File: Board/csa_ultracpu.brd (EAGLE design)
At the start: 160 x 100.1 mm, 131 parts, among them IC1 RAMSOCK32TO512KSOP, IC10 RAMSOCK32TO512KSOP, IC11 74HCT574D, IC12 74HCT574D, IC13 74HCT244DW, IC14 74HCT14D, IC15 74HCT157D, IC18 74LS06D, IC19 74HCT244DW, IC2 74LS245DW, IC3 74LS245DW, IC4 74LS245DW, IC5 74LS245DW, IC6 74ACT138D, IC7 74LS245DW, IC8 MAX3421E, IC9 74LS166D, P1 CSABUS, Q2 32kHz, Q3 12MHz, X2 D-SUB15-HDR15RA

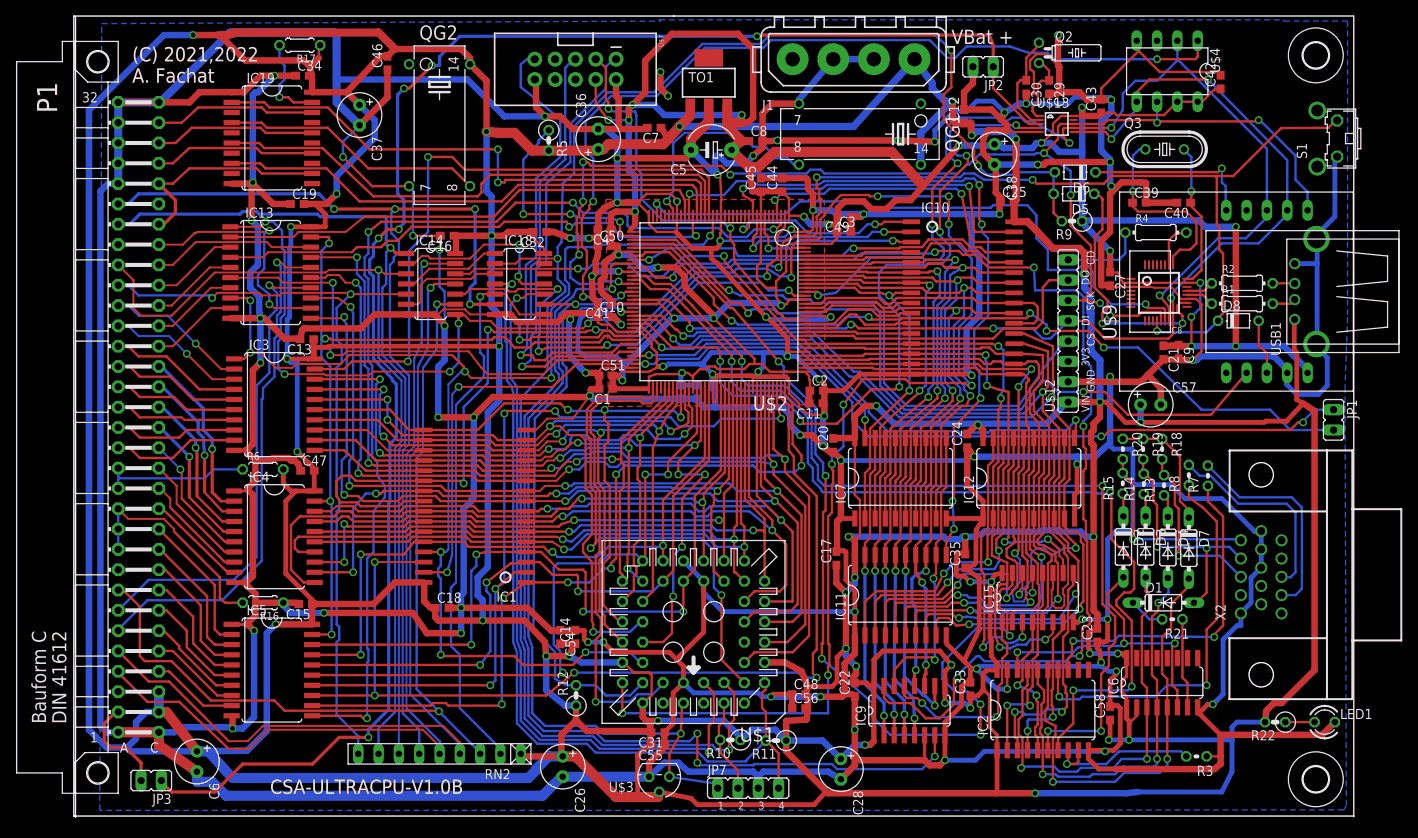
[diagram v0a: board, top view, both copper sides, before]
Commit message: update board to 1.3C
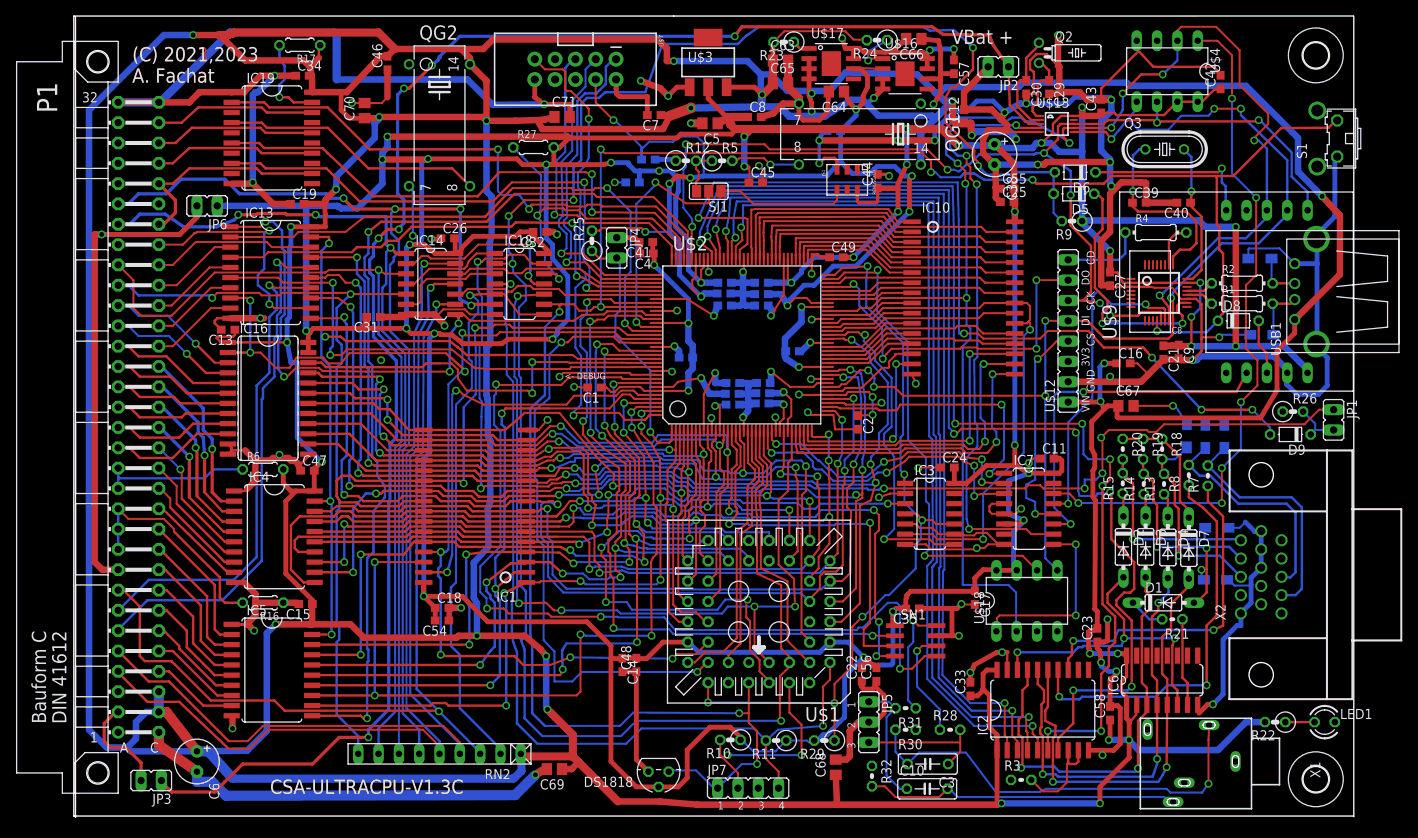
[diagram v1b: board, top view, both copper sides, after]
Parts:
- removed C20, C52: 0.1u, rcl:C0603
- removed C28, C36, C37: 22u, rcl:E2,5-6
- removed C50, C51, C53: 1u, rcl:C0603
- removed IC11, IC12: 74HCT574D, 74xx-eu:SO20W
- removed IC15: 74HCT157D, 74xx-eu:SO16
- removed IC9: 74LS166D, 74xx-eu:SO16
- removed J1: (no value), con-amp:350211
- removed TO1: LM2937SOT-3.3V, csa:SOT223
- added C100, C101, C102, C103, C104, C105, C106, C107, C108, C109, C110, C111, C112, C113: 0.1u, rcl:C0603
- added C120, C121, C123: 1u, rcl:C0603
- added C63, C64, C65, C66, C67, C68, C69, C70, C71: 22u, rcl:C0805
- added D9: 1N4148, diode:D-5
- added DS1818: DS1818, csa:TO92
- added IC16: 74LVC8T245SO24, csa:SO24L
- added JP4, JP6: (no value), jumper:JP1
- added JP5: (no value), jumper:JP2
- added JS1: RENOSCXLH, csa:RENJS6
- added R23, R24, R26: 10k, rcl:0207/2V
- added R25: 4k7, rcl:0207/2V
- added R27: 10k, rcl:0204/5
- added R28, R31: 100, rcl:0204V
- added R29: 330, rcl:0207/2V
- added R30, R32: 680, rcl:0204V
- added SJ1: (no value), jumper:SJ_2
- added SN1: MCP48X2, csa:SOIC8
- added U$10, U$11, U$14, U$15, U$5, U$6, U$8: PESD5V0L1BA, csa:SOD323
- added U$16: AP2132B-1.2, csa:PSOP-8-FIXED
- added U$17: AP2132B-2.5, csa:PSOP-8-FIXED
- added U$18: SPIFLASH, csa:DIL08
- added X1: SJ1-3513N, con-lumberg:1503_09
- C1, C14, C4: value 0.1u -> 1u
- C10: device rcl:C0603 -> rcl:C050-025X075
- C11: value 1u -> 0.1u
- C26: value 47u -> 0.1u; device rcl:E2,5-6 -> rcl:C0603
- C3: value 0.1u -> 1u; device rcl:C0603 -> rcl:C050-025X075
- C5: value 47u -> 22u; device rcl:E5-6 -> rcl:C0805
- C57: value 22u -> 1u; device rcl:E2,5-6 -> rcl:C0603
- IC14: value 74HCT14D -> 74LVC14
- IC18: value 74LS06D -> 74LVC06
- IC2, IC4, IC5: value 74LS245DW -> 74HCT245DW
- IC3: value 74LS245DW -> 74LS125D; device 74xx-eu:SO20W -> 74xx-eu:SO14
- IC6: value 74ACT138D -> 74HC138D
- IC7: value 74LS245DW -> 74S138D; device 74xx-eu:SO20W -> 74xx-eu:SO16
- R12: value 1k -> 1k5
- U$2: value XC95288XLTQ144 -> XC3S250E
- U$3: value DS1813 -> LDI1117; device csa:TO92 -> csa:SOT223
- moved U$3 88.2 mm to (78.7, 93.7), turned to 0 degrees
- moved C16 86.0 mm to (130.6, 56.1), turned to 0 degrees
- moved IC3 83.0 mm to (106.4, 37.3)
- moved C55 82.1 mm to (116.0, 77.9), turned to 0 degrees
- moved C10 71.4 mm to (106.0, 2.94)
- moved R12 68.2 mm to (75.9, 81.4), turned to 0 degrees
- moved C26 67.6 mm to (46.1, 71.8), turned to 0 degrees
- moved C3 67.3 mm to (106.1, 6.03), turned to 180 degrees
- moved C31 62.9 mm to (36.8, 61.9)
- moved C57 48.9 mm to (109.4, 93.2), turned to 270 degrees
- moved C11 29.7 mm to (121.0, 44.2), turned to 0 degrees
- moved R3 22.1 mm to (117.8, 4.05), turned to 0 degrees
- moved R5 21.8 mm to (80.4, 81.4), turned to 0 degrees
- moved C48 20.6 mm to (69.7, 18.4), turned to 90 degrees
- moved C17 18.0 mm to (112.0, 26.8), turned to 270 degrees
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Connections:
- removed net /CHROMADDR: IC7.19, U$2.68
- removed net /DENA: IC15.15, U$2.41
- removed net /RAMCS: IC10.22, IC10.24, U$2.126
- removed net /SRLOAD: IC9.15, U$2.46
- removed net BG0: IC12.15, IC15.2
- removed net BG1: IC12.14, IC15.5
- removed net BG2: IC12.13, IC15.11
- removed net BG3: IC12.12, IC15.14
- removed net COLORLD: IC12.11, U$2.61
- removed net COLORLD2: U$2.16
- removed net FA18: IC1.1, IC5.12, U$2.107
- removed net FG0: IC12.19, IC15.3
- removed net FG1: IC12.18, IC15.6
- removed net FG2: IC12.17, IC15.10
- removed net FG3: IC12.16, IC15.13
- removed net PHI2_IO: R5.1, U$2.38
- removed net PIXELS: IC15.1, IC9.13
- removed net PXL0: IC11.19, IC7.18, IC9.2
- removed net PXL1: IC11.18, IC7.17, IC9.3
- removed net PXL2: IC11.17, IC7.16, IC9.4
- removed net PXL3: IC11.16, IC7.15, IC9.5
- removed net PXL4: IC11.15, IC7.14, IC9.10
- removed net PXL5: IC11.14, IC7.13, IC9.11
- removed net PXL6: IC11.13, IC7.12, IC9.12
- removed net PXL7: IC11.12, IC7.11, IC9.14
- removed net PXLLD: IC11.11, U$2.26
- removed net RAMA11: IC10.25, IC7.9, U$2.131
- removed net RAMA3: IC10.9, U$2.125
- removed net RAMA5: IC10.7, IC7.3, U$2.132
- removed net RAMA9: IC10.26, IC7.7, U$2.133
- removed net SPI_IN1: IC8.15, U$13.7, U$2.129, U$4.2, U$9.1_3
- removed net SPI_OUT: IC8.16, U$12.DI, U$13.6, U$2.54, U$4.5, U$9.1_2
- removed net SRCLK: IC9.7, U$2.45
- new net /FPGA_BOOT: IC7.9, U$18.1
- new net /LDAC: SN1.5, U$2.135
- new net /RAMCS/M1: IC10.22, IC10.24, IC3.6, U$2.60
- new net 50MCAN: R12.2, R5.1, SJ1.3
- new net 50MSMD: JS1.4, SJ1.1
- new net BV33: JP6.2, P1.A9
- new net DEBUG: U$2.134
- new net DONE: IC3.1, IC3.10, IC3.4, R29.1, U$1.40, U$2.72
- new net FA18/HSWAP: IC1.1, IC3.3, IC5.12, U$2.143
- new net GRAPHIC5V: IC18.13, JP1.1
- new net INIT_B: U$2.40
- new net M2: IC3.8, U$2.57
- new net N$12: R24.1, U$16.1
- new net N$21: D9.C, JP1.2, R26.2
- new net N$22: R28.1, SN1.6
- new net N$23: C3.2, R30.2, X1.2
- new net N$26: R31.1, SN1.8
- new net N$27: C10.1, JP5.1, R31.2
- new net N$28: C10.2, R32.2, X1.3
- new net N$42: C3.1, JP5.3, R28.2
- new net N$6: R23.1, U$17.1
- new net N$7: QG1.8, R5.2
- new net PROG_B: JP4.2, R25.1, U$2.1
- new net RAMA11/VS2: IC10.25, U$2.67
- new net RAMA3/M0: IC10.9, U$2.62
- new net RAMA5/VS1: IC10.7, U$2.68
- new net RAMA9/VS0: IC10.26, U$2.70
- new net SPISELA/CSO_B: IC7.1, U$2.39
- new net SPISELB: IC7.2, U$2.26
- new net SPISELC: IC7.3, U$2.25
- new net SPI_ACLK: SN1.3, U$2.17
- new net SPI_AMOSI: SN1.4, U$2.16
- new net SPI_CLK/CCLK: U$18.6, U$2.71
- new net SPI_MISO/DIN: IC8.15, U$13.7, U$18.2, U$2.63, U$4.2, U$9.1_3
- new net SPI_MOSI: IC8.16, U$12.DI, U$13.6, U$18.5, U$2.44, U$4.5, U$9.1_2
- new net SPI_NAUDIO: SN1.2, U$2.116
- new net V12: C102.2, C105.2, C108.2, C111.2, C57.2, C66.1, U$16.6, U$2.115, U$2.45, U$2.80, U$2.9
- new net V25: C101.1, C104.1, C109.1, C112.1, C121.1, C123.1, C64.1, R25.2, U$16.2, U$17.6, U$2.102, U$2.137, U$2.30, U$2.65, U$7.4
- net /BE_DOUT: now also IC16.22, U$2.131; no longer IC3.19, U$2.21
- net /BE_OUT: now also U$2.130; no longer U$2.64
- net /FRAMSEL: now also U$2.124; no longer U$2.2
- net /IOSEL: now also U$2.132; no longer U$2.69
- net /IRQ: now also U$2.22
- net /MEMSEL: now also U$2.112; no longer U$2.25
- net /RAMWE: now also U$2.82; no longer U$2.44
- net /RES: now also DS1818.1, U$2.117; no longer U$2.143, U$3.1
- net 50M: now also SJ1.2, U$2.122; no longer QG1.8, U$2.30
- net A0: now also U$2.18; no longer U$2.104
- net A1: now also U$2.56; no longer U$2.103
- net A10: now also U$2.12; no longer U$2.93
- net A11: now also U$2.141; no longer U$2.92
- net A12: now also U$2.128; no longer U$2.91
- net A13: now also U$2.136; no longer U$2.87
- net A14: now also U$2.120; no longer U$2.88
- net A15: now also U$2.129; no longer U$2.85
- net A2: now also U$2.48; no longer U$2.102
- net A3: now also U$2.41; no longer U$2.101
- net A4: now also U$2.47; no longer U$2.100
- net A5: now also U$2.36; no longer U$2.98
- net A6: now also U$2.38; no longer U$2.97
- net A7: now also U$2.24; no longer U$2.96
- net A8: now also U$2.29; no longer U$2.95
- net A9: now also U$2.10; no longer U$2.94
- net BD0: now also IC16.3; no longer IC3.2
- net BD1: now also IC16.4; no longer IC3.3
- net BD2: now also IC16.5; no longer IC3.4
- net BD3: now also IC16.6; no longer IC3.5
- net BD4: now also IC16.7; no longer IC3.6
- net BD5: now also IC16.8; no longer IC3.7
- net BD6: now also IC16.9; no longer IC3.8
- net BD7: now also IC16.10; no longer IC3.9
- net BE_IN: now also U$2.119; no longer U$2.140
- net BOUT: now also U$2.93; no longer IC15.7
- net C2PHI2: now also U$2.106; no longer U$2.22
- net C8PHI2: now also U$2.105; no longer U$2.23
- net CPHI2: now also U$2.113; no longer U$2.24
- net D0: now also IC16.21, U$2.3; no longer IC3.18, U$2.86
- net D1: now also IC16.20, U$2.2; no longer IC3.17, U$2.83
- net D2: now also IC16.19, U$2.15; no longer IC3.16, U$2.82
- net D3: now also IC16.18, U$2.4; no longer IC3.15, U$2.81
- net D4: now also IC16.17, U$2.14; no longer IC3.14, U$2.80
- net D5: now also IC16.16, U$2.7; no longer IC3.13, U$2.79
- net D6: now also IC16.15, U$2.8; no longer IC3.12, U$2.78
- net D7: now also IC16.14, U$2.5; no longer IC3.11, U$2.77
- net E: now also U$2.20; no longer U$2.142
- net EXTIO: now also U$2.114; no longer U$2.128
- net FA15: now also U$2.139; no longer U$2.71
- net FA16: now also U$2.140; no longer U$2.105
- net FA17: now also U$2.142; no longer U$2.106
- net FA19: now also U$2.104; no longer U$2.3
- net GND: now also C100.1, C101.2, C102.1, C103.2, C104.2, C105.1, C106.1, C107.1, C108.1, C109.2, C110.2, C111.1, C112.2, C113.1, C120.2, C121.2, C123.2, C26.1, C5.2, C57.1, C63.2, C64.2, C65.2, C66.2, C67.2, C68.2, C69.2, C70.2, C71.2, DS1818.3, IC16.11, IC16.12, IC16.13, IC3.2, IC3.5, IC3.7, IC3.9, IC7.4, IC7.5, IC7.8, JP4.1, JP5.2, JS1.3, R12.1, R26.1, R30.1, R32.1, SN1.7, U$10.1, U$11.1, U$14.1, U$15.1, U$16.7, U$16.8, U$17.7, U$17.8, U$18.4, U$2.11, U$2.118, U$2.127, U$2.133, U$2.19, U$2.27, U$2.37, U$2.46, U$2.55, U$2.61, U$2.73, U$3.1, U$5.1, U$6.1, U$8.1, X1.1; no longer C10.1, C20.1, C26.-, C28.-, C3.2, C36.-, C37.-, C5.-, C50.1, C51.1, C52.2, C53.1, C57.-, IC11.1, IC11.10, IC12.1, IC12.10, IC15.8, IC3.10, IC7.1, IC7.10, IC9.6, IC9.8, J1.2, J1.3, TO1.2, U$2.108, U$2.114, U$2.123, U$2.144, U$2.18, U$2.29, U$2.36, U$2.47, U$2.62, U$2.72, U$2.89, U$3.3
- net GOUT: now also U$2.94; no longer IC15.9
- net GRAPHIC: now also IC18.12, R27.1, U$2.107; no longer JP1.1, U$2.70
- net HSYNC: now also U$2.98; no longer U$2.48
- net IOINH: now also U$2.111; no longer U$2.117
- net IOUT: now also U$2.92; no longer IC15.4
- net N$17: now also U$8.2
- net N$18: now also U$10.2
- net N$19: now also U$11.2
- net N$24: now also U$6.2
- net N$25: now also U$5.2
- net N$35: now also U$14.2
- net N$36: now also U$15.2
- net PET_VSYNC: now also D9.A, U$2.91; no longer JP1.2, U$2.43
- net PHI2: now also U$2.126; no longer R12.2, U$2.57
- net R/-W: now also IC16.2, U$2.125; no longer IC3.1, U$2.20
- net RAMA0: now also U$2.52; no longer U$2.119
- net RAMA1: now also U$2.54; no longer U$2.120
- net RAMA10: now also U$2.58; no longer IC7.8, U$2.124
- net RAMA12: now also U$2.81; no longer U$2.138
- net RAMA13: now also U$2.77; no longer U$2.137
- net RAMA14: now also U$2.83; no longer U$2.7
- net RAMA15: now also U$2.87; no longer U$2.10
- net RAMA16: now also U$2.86; no longer U$2.9
- net RAMA17: now also U$2.85; no longer U$2.4
- net RAMA18: now also U$2.88; no longer U$2.11
- net RAMA2: now also U$2.59; no longer U$2.121
- net RAMA4: now also U$2.66; no longer IC7.2, U$2.130
- net RAMA6: now also U$2.74; no longer IC7.4, U$2.134
- net RAMA7: now also U$2.76; no longer IC7.5, U$2.136
- net RAMA8: now also U$2.75; no longer IC7.6, U$2.135
- net RAMD0: now also U$2.50; no longer IC11.2, IC12.2, U$2.116
- net RAMD1: now also U$2.43; no longer IC11.3, IC12.3, U$2.113
- net RAMD2: now also U$2.35; no longer IC11.4, IC12.4, U$2.111
- net RAMD3: now also U$2.32; no longer IC11.5, IC12.5, U$2.110
- net RAMD4: now also U$2.33; no longer IC11.6, IC12.6, U$2.112
- net RAMD5: now also U$2.34; no longer IC11.7, IC12.7, U$2.115
- net RAMD6: now also U$2.51; no longer IC11.8, IC12.8, U$2.58
- net RAMD7: now also U$2.53; no longer IC11.9, IC12.9, U$2.59
- net RDY: now also U$2.31
- net ROUT: now also U$2.96; no longer IC15.12
- net SPI_CLK: now also U$2.103; no longer U$2.50
- net SPI_IN3: now also U$2.69; no longer U$2.118
- net SPI_NFLASH: now also IC7.14; no longer U$2.52
- net SPI_NSEL2: now also IC7.13; no longer U$2.34
- net SPI_NSEL3: now also IC7.12; no longer U$2.39
- net SPI_NSEL4: now also IC7.11; no longer U$2.40
- net SPI_NSEL5: now also IC7.10; no longer U$2.60
- net SYNC: now also U$2.123; no longer U$2.27
- net TCK: now also U$2.110; no longer U$2.67
- net TDI: now also U$2.144; no longer U$2.63
- net TDO: now also U$2.109; no longer U$2.122
- net TMS: now also U$2.108; no longer U$2.65
- net V33: now also C100.2, C103.1, C106.2, C107.2, C110.1, C113.2, C120.1, C14.1, C17.1, C18.1, C22.2, C24.2, C25.2, C26.2, C31.2, C32.2, C35.2, C48.2, C5.1, C54.2, C55.2, C56.2, DS1818.2, IC1.32, IC10.32, IC14.14, IC16.23, IC16.24, IC18.14, IC3.14, IC7.16, IC7.6, JP6.1, JS1.6, R10.1, R11.1, R27.2, R29.2, SN1.1, U$1.37, U$1.9, U$18.7, U$18.8, U$2.100, U$2.121, U$2.13, U$2.138, U$2.28, U$2.49, U$2.64, U$2.79, U$3.2; no longer C10.2, C3.1, C5.+, C50.2, C51.2, C52.1, C53.2, TO1.3, U$2.1, U$2.109, U$2.127, U$2.141, U$2.37, U$2.55, U$2.73, U$2.8, U$2.84, U$7.4
- net VCC: now also C63.1, C65.1, C67.1, C68.1, C69.1, C70.1, C71.1, IC16.1, R23.2, R24.2, U$16.3, U$16.4, U$17.2, U$17.3, U$17.4, U$3.3; no longer C14.1, C17.1, C18.1, C20.2, C22.2, C24.2, C25.2, C26.+, C28.+, C31.2, C32.2, C35.2, C36.+, C37.+, C48.2, C54.2, C55.2, C56.2, C57.+, IC1.32, IC10.32, IC11.20, IC12.20, IC14.14, IC15.16, IC18.14, IC3.20, IC7.20, IC9.1, IC9.16, IC9.9, J1.4, R10.1, R11.1, R12.1, R5.2, TO1.1, U$1.37, U$1.40, U$1.9, U$3.2
- net VDA: now also U$2.21; no longer U$2.75
- net VPA: now also U$2.23; no longer U$2.74
- net VPB: now also U$2.6
- net VSYNC: now also U$2.97; no longer U$2.49
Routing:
- net GND: track 1758.0 -> 862.5 mm, vias 77 -> 69
- net V33: track 458.0 -> 911.0 mm, vias 24 -> 45
- net VCC: track 1226.0 -> 1012.0 mm, vias 40 -> 29
- net V25: track 0.00 -> 209.1 mm, vias 0 -> 11
- net SPI_MISO/DIN: track 0.00 -> 185.5 mm, vias 0 -> 9
- net GRAPHIC5V: track 0.00 -> 154.6 mm, vias 0 -> 7
- net SPI_MOSI: track 0.00 -> 145.3 mm, vias 0 -> 8
- net /SRLOAD: track 142.1 -> 0.00 mm, vias 6 -> 0
- net SPI_OUT: track 138.7 -> 0.00 mm, vias 6 -> 0
- net SRCLK: track 126.6 -> 0.00 mm, vias 4 -> 0
- net SPI_IN1: track 125.1 -> 0.00 mm, vias 6 -> 0
- net /DENA: track 121.3 -> 0.00 mm, vias 6 -> 0
- net V12: track 0.00 -> 118.0 mm, vias 0 -> 5
- net /LDAC: track 0.00 -> 117.8 mm, vias 0 -> 4
- net FA18/HSWAP: track 0.00 -> 114.6 mm, vias 0 -> 8
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- added copper zone on layer 15, net GND
- added copper zone on layer 2, net GND
- removed copper zone on layer 16, net GND
- removed copper zone on layer 1, net V33
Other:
- board text added: "(C) 2021,2023 A. Fachat"
- board text added: "(C) 2023 A. Fachat"
- board text added: "<- DEBUG"
- board text added: "<-INIT_B"
- board text added: "CSA-ULTRACPU-V1.3C"
- board text removed: "(C) 2021 A. Fachat"
- board text removed: "(C) 2021,2022 A. Fachat"
- board text removed: "CSA-ULTRACPU-V1.0B"

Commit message: update board to 2.0b from internal repo
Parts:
- removed C23: 0.1u, rcl:C0603
- removed C63: 22u, rcl:C0805
- removed QG2: 16MHz, crystal:SG51
- removed R21: 2k, rcl:0204V
- removed R23: 10k, rcl:0207/2V
- removed R3: 10k, rcl:0204V
- removed U$17: AP2132B-2.5, csa:PSOP-8-FIXED
- added C20, C28, C36, C37: 0.1u, rcl:C0603
- added D10: 1N4148DO35-7, diode:DO35-7
- added JP10, JP11, JP8, JP9: PIN, csa:PIN
- IC3: value 74LS125D -> 74LVC125
- IC6: value 74HC138D -> 74LVC1G04DBV; device 74xx-eu:SO16 -> 74xx-little-us:SOT23-5
- IC7: value 74S138D -> 74LVC138
- U$2: value XC3S250E -> XC6SLX9-TQG144
- moved IC6 71.1 mm to (64.4, 14.3)
- moved R25 60.3 mm to (124.5, 72.2), turned to 0 degrees
- moved JP4 53.1 mm to (120.3, 73.6)
- moved C105 8.24 mm to (89.1, 56.0), turned to 0 degrees
- moved C104 7.30 mm to (90.4, 59.5), turned to 180 degrees
- moved D1 4.80 mm to (136.6, 21.5), turned to 270 degrees
- moved C102 4.37 mm to (85.1, 63.4), turned to 270 degrees
- moved C109 4.33 mm to (77.9, 50.2), turned to 270 degrees
- moved C108 4.07 mm to (78.6, 56.2), turned to 180 degrees
- moved C107 3.84 mm to (90.8, 54.1)
- moved C2 3.49 mm to (94.1, 47.5), turned to 0 degrees
- moved C112 2.72 mm to (87.2, 50.2), turned to 270 degrees
- moved C106 1.93 mm to (75.2, 55.0)
- moved C110 1.77 mm to (80.2, 50.2), turned to 270 degrees
- moved C1 1.59 mm to (64.5, 54.7)
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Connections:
- removed net /RAMCS/M1: IC10.22, IC10.24, IC3.6, U$2.60
- removed net C16M: IC19.4, QG2.8
- removed net DEBUG: U$2.134
- removed net INIT_B: U$2.40
- removed net INTENSITY: D7.A, IC2.15, IC6.5
- removed net IOUT: IC2.5, U$2.92
- removed net M2: IC3.8, U$2.57
- removed net N$1: IC2.8, IC2.9, R3.2
- removed net N$6: R23.1, U$17.1
- removed net RAMA11/VS2: IC10.25, U$2.67
- removed net RAMA3/M0: IC10.9, U$2.62
- removed net RAMA5/VS1: IC10.7, U$2.68
- removed net RAMA9/VS0: IC10.26, U$2.70
- removed net SPI_CLK: IC8.13, U$12.SCK, U$13.8, U$2.103, U$4.6, U$9.1_1
- removed net V25: C101.1, C104.1, C109.1, C112.1, C121.1, C123.1, C64.1, R25.2, U$16.2, U$17.6, U$2.102, U$2.137, U$2.30, U$2.65, U$7.4
- new net /BE: IC6.2, U$2.100
- new net /RAMCS: IC10.22, IC10.24, U$2.59
- new net BE: IC6.4, U$1.40
- new net IBLUE: D7.A, IC2.15
- new net IBOUT: IC2.5, U$2.93
- new net IGOUT: IC2.8, U$2.74
- new net IGREEN: D1.A, IC2.12
- new net IRED: D10.A, IC2.11
- new net IROUT: IC2.9, U$2.105
- new net RAMA11: IC10.25, U$2.62
- new net RAMA3: IC10.9, IC3.6, U$2.60
- new net RAMA5: IC10.7, U$2.66
- new net RAMA9: IC10.26, U$2.69
- net /BE_DOUT: now also U$2.133; no longer U$2.131
- net /BE_OUT: now also U$2.132; no longer U$2.130
- net /FRAMSEL: now also U$2.120; no longer U$2.124
- net /IOSEL: now also U$2.134; no longer U$2.132
- net /IRQ: now also JP11.1, U$2.23; no longer U$2.22
- net /LDAC: now also U$2.138; no longer U$2.135
- net /RES: now also IC3.8
- net 50M: now also U$2.123; no longer U$2.122
- net A0: now also U$2.17; no longer U$2.18
- net A10: now also U$2.11; no longer U$2.12
- net A11: now also U$2.142; no longer U$2.141
- net A12: now also U$2.127; no longer U$2.128
- net A13: now also U$2.139; no longer U$2.136
- net A14: now also U$2.119; no longer U$2.120
- net A15: now also U$2.131; no longer U$2.129
- net A2: now also U$2.45; no longer U$2.48
- net A3: now also U$2.43; no longer U$2.41
- net A4: now also U$2.44; no longer U$2.47
- net A5: now also U$2.40; no longer U$2.36
- net A6: now also U$2.41; no longer U$2.38
- net A7: now also U$2.26; no longer U$2.24
- net A8: now also U$2.30; no longer U$2.29
- net BE_IN: now also U$2.118; no longer U$2.119
- net BLUE: no longer IC6.4
- net BOUT: now also U$2.94; no longer U$2.93
- net C2PHI2: now also U$2.104; no longer U$2.106
- net C8PHI2: now also U$2.102; no longer U$2.105
- net CPHI2: now also U$2.114; no longer U$2.113
- net D0: now also U$2.2; no longer U$2.3
- net D1: now also U$2.1; no longer U$2.2
- net D2: now also U$2.14; no longer U$2.15
- net D3: now also U$2.5; no longer U$2.4
- net D4: now also U$2.12; no longer U$2.14
- net D5: now also U$2.8; no longer U$2.7
- net D6: now also U$2.9; no longer U$2.8
- net D7: now also U$2.6; no longer U$2.5
- net DONE: now also U$2.71; no longer U$1.40, U$2.72
- net E: now also U$2.21; no longer U$2.20
- net EXTIO: now also U$2.115; no longer U$2.114
- net FA15: now also U$2.140; no longer U$2.139
- net FA16: now also U$2.141; no longer U$2.140
- net FA17: now also U$2.143; no longer U$2.142
- net FA18/HSWAP: now also U$2.144; no longer U$2.143
- net FA19: now also U$2.101; no longer U$2.104
- net GND: now also C20.2, C28.2, C36.2, C37.2, IC6.3, U$2.108, U$2.113, U$2.13, U$2.130, U$2.136, U$2.25, U$2.3, U$2.49, U$2.54, U$2.68, U$2.77, U$2.91, U$2.96; no longer C23.1, C63.2, IC6.8, QG2.7, R3.1, U$17.7, U$17.8, U$2.11, U$2.118, U$2.127, U$2.133, U$2.19, U$2.27, U$2.37, U$2.46, U$2.55, U$2.61, U$2.73, U$2.90, U$2.99
- net GOUT: now also U$2.95; no longer U$2.94
- net GRAPHIC: now also U$2.137; no longer U$2.107
- net GREEN: no longer IC6.3
- net HSYNC: now also U$2.99; no longer U$2.98
- net N$11: now also IC19.4
- net N$14: now also D1.C; no longer D7.C, R18.1, R20.1
- net N$16: now also D7.C, R18.1; no longer IC6.7, R21.1
- net N$18: no longer D1.A
- net N$20: now also D10.C, R20.1; no longer D1.C, R21.2
- net PET_VSYNC: now also U$2.92; no longer U$2.91
- net PHI2: now also JP9.1
- net PROG_B: now also U$2.37; no longer U$2.1
- net R/-W: now also U$2.124; no longer U$2.125
- net RAMA0: now also U$2.50; no longer U$2.52
- net RAMA1: now also U$2.55; no longer U$2.54
- net RAMA10: now also U$2.57; no longer U$2.58
- net RAMA13: now also U$2.80; no longer U$2.77
- net RAMA16: now also U$2.85; no longer U$2.86
- net RAMA17: now also U$2.84; no longer U$2.85
- net RAMA2: now also U$2.58; no longer U$2.59
- net RAMA4: now also U$2.61; no longer U$2.66
- net RAMA6: now also U$2.75; no longer U$2.74
- net RAMA7: now also U$2.79; no longer U$2.76
- net RAMA8: now also U$2.78; no longer U$2.75
- net RAMD0: now also U$2.47; no longer U$2.50
- net RAMD1: now also U$2.46; no longer U$2.43
- net RAMD2: now also U$2.39; no longer U$2.35
- net RAMD3: now also U$2.33; no longer U$2.32
- net RAMD4: now also U$2.34; no longer U$2.33
- net RAMD5: now also U$2.35; no longer U$2.34
- net RAMD6: now also U$2.48; no longer U$2.51
- net RAMD7: now also U$2.51; no longer U$2.53
- net RDY: now also U$2.32; no longer U$2.31
- net RED: no longer IC6.6
- net ROUT: now also U$2.97; no longer U$2.96
- net SPISELA/CSO_B: now also U$2.38; no longer U$2.39
- net SPISELB: now also U$2.29; no longer U$2.26
- net SPISELC: now also U$2.27; no longer U$2.25
- net SPI_ACLK: now also U$2.16; no longer U$2.17
- net SPI_AMOSI: now also U$2.15; no longer U$2.16
- net SPI_CLK/CCLK: now also IC8.13, U$12.SCK, U$13.8, U$2.70, U$4.6, U$9.1_1; no longer U$2.71
- net SPI_IN3: now also U$2.67; no longer U$2.69
- net SPI_MISO/DIN: now also U$2.65; no longer U$2.63
- net SPI_MOSI: now also U$2.64; no longer U$2.44
- net SPI_NFLASH: now also JP10.1
- net SYNC: now also U$2.121; no longer U$2.123
- net TCK: now also U$2.109; no longer U$2.110
- net TDI: now also U$2.110; no longer U$2.144
- net TDO: now also U$2.106; no longer U$2.109
- net TMS: now also U$2.107; no longer U$2.108
- net V12: now also U$2.128, U$2.19, U$2.28, U$2.52, U$2.89; no longer U$2.115, U$2.45, U$2.80, U$2.9
- net V33: now also C101.1, C104.1, C109.1, C112.1, C121.1, C123.1, C20.1, C28.1, C36.1, C37.1, C64.1, IC6.5, R25.2, U$16.2, U$2.103, U$2.122, U$2.125, U$2.129, U$2.135, U$2.18, U$2.20, U$2.31, U$2.36, U$2.4, U$2.53, U$2.63, U$2.76, U$2.86, U$2.90, U$7.4; no longer U$2.100, U$2.121, U$2.13, U$2.138, U$2.28, U$2.49, U$2.64, U$2.79
- net VCC: no longer C23.2, C63.1, IC6.1, IC6.16, IC6.2, QG2.14, R23.2, U$17.2, U$17.3, U$17.4
- net VDA: now also U$2.22; no longer U$2.21
- net VPA: now also U$2.24; no longer U$2.23
- net VPB: now also JP8.1, U$2.7; no longer U$2.6
- net VSYNC: now also U$2.98; no longer U$2.97
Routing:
- net V25: track 209.1 -> 0.00 mm, vias 11 -> 0
- net V33: track 911.0 -> 1119.4 mm, vias 45 -> 54
- net SPI_CLK: track 143.6 -> 0.00 mm, vias 9 -> 0
- net IROUT: track 0.00 -> 123.0 mm, vias 0 -> 2
- net SPI_CLK/CCLK: track 60.1 -> 178.4 mm, vias 2 -> 11
- net IBOUT: track 0.00 -> 109.3 mm, vias 0 -> 2
- net IOUT: track 108.9 -> 0.00 mm, vias 2 -> 0
- net /BE: track 0.00 -> 96.5 mm, vias 0 -> 2
- net IGOUT: track 0.00 -> 93.2 mm, vias 0 -> 2
- net /RAMCS/M1: track 70.1 -> 0.00 mm, vias 2 -> 0
- net GND: track 862.5 -> 930.4 mm, vias 69 -> 76
- net RAMA3: track 0.00 -> 66.4 mm, vias 0 -> 4
- net IBLUE: track 0.00 -> 59.7 mm, vias 0 -> 3
- net INTENSITY: track 55.5 -> 0.00 mm, vias 2 -> 0
- net /RES: track 266.0 -> 308.9 mm, vias 8 -> 10
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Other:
- board text added: "(C) 2021,2024 A. Fachat"
- board text added: "/ABRT"
- board text added: "/FLASH"
- board text added: "/IRQ"
- board text added: "/NMI"
- board text added: "/RES"
- board text added: "CSA-ULTRACPU-V2.0B"
- board text added: "GND"
- board text added: "PHI2"
- board text added: "VPB"
- board text removed: "(C) 2021,2023 A. Fachat"
- board text removed: "<-INIT_B"
- board text removed: "CSA-ULTRACPU-V1.3C"
